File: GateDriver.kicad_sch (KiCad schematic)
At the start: 0 parts

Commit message: add gate driver
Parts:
- added C15: 10nF, symbol Device:C_Small
- added C16, C19: 220nF, symbol Device:C_Small
- added C17: 4.7uF, symbol Device:C_Small
- added C18: 2.2uF, symbol Device:C_Small
- added R28, R31, R32, R34, R35, R36, R37: 1k, symbol Device:R_Small
- added R38, R39: 10k, symbol Device:R_Small
- added U4: 2ED4820EMXUMA2, custom_footprints:2ed4820emxuma2, symbol custom_symbols:2ED4820EMXUMA2
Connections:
- new net: R28.2, U4.1 (SAFESTATEN)
- new net: R36.2, U4.6 (MISO)
- new net: R31.2, U4.2 (INTERRUPT)
- new net: R35.2, U4.5 (MOSI)
- new net: R34.2, R39.1, U4.4 (CSN)
- new net: R32.2, U4.3 (SCLK)
- new net: R37.2, U4.7 (ENABLE)
- new net: C15.1, R38.1
- new net: R38.2, U4.9 (CSO)
- new net +3V3: R39.2, U4.8 (VDD)
- new net BAT+: C16.1, C17.1, C18.2, U4.24 (VBAT)
- new net GATE_A: U4.18 (GA)
- new net GD_EN: R37.1
- new net GD_INT: R31.1
- new net GND: C16.2, C17.2, U4.12 (AGND), U4.13 (GND), U4.19 (CPGND), U4.25 (EPAD)
- new net IS_N: U4.10 (ISN)
- new net IS_P: U4.11 (ISP)
- new net SOURCE_A: U4.17 (SA)
- new net SPI2_MISO: R36.1
- new net SPI2_MOSI: R35.1
- new net SPI2_SCLK: R32.1
- new net cph: C19.2, U4.22 (CPH)
- new net cpl: C19.1, U4.21 (CPL)
- new net vcp: C18.1, U4.23 (VCP)
- new net ~{GD_SAFE}: R28.1
- new net ~{SPI2_CS}: R34.1
- no-connect marks 0 -> 2

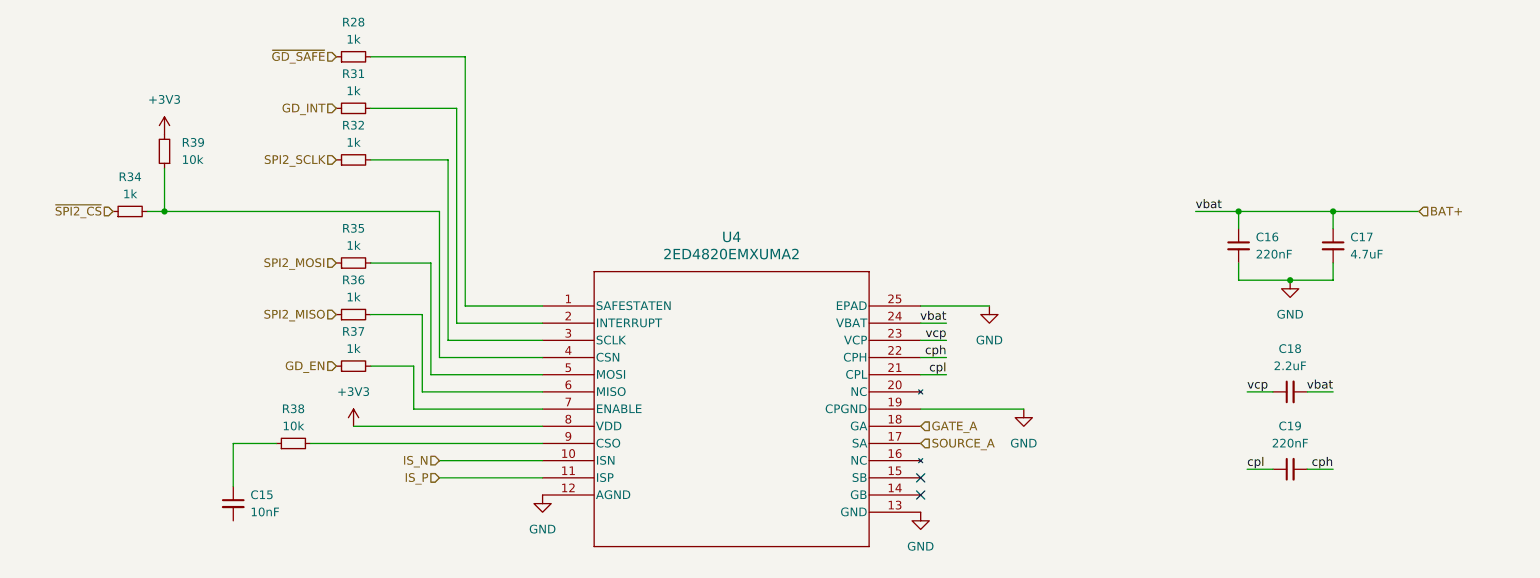
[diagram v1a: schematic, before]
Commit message: finish protection sheet
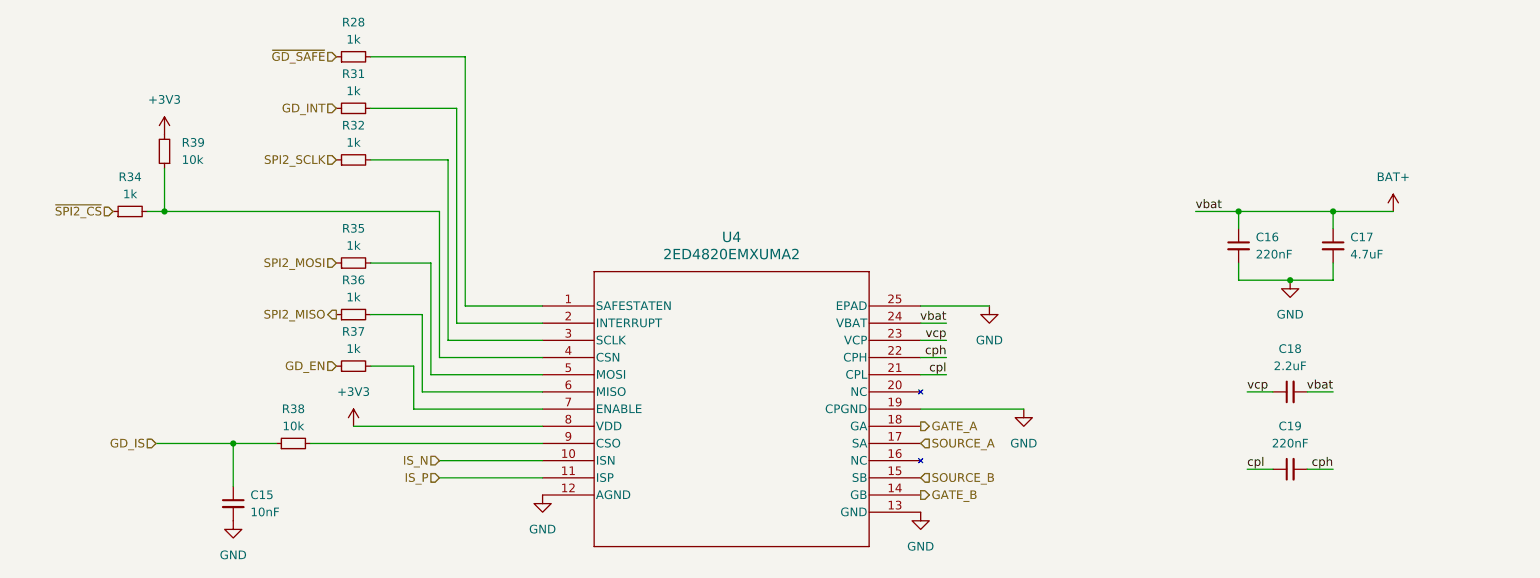
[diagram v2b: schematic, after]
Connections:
- net GND: now also C15.2
- net GD_IS: now reaches C15.1, R38.1
- net GATE_B: now reaches U4.14 (GB)
- net SOURCE_B: now reaches U4.15 (SB)
- no-connect marks 2 -> 0
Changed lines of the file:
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@@
+	)
+	(junction
+		(at 101.6 104.14)
+		(diameter 0)
+		(color 0 0 0 0)
+	)
+	(junction
+		(at 264.16 69.85)
+		(diameter 0)
+		(color 0 0 0 0)
 	)
 	(junction
@@
 	)
 	(junction
-		(at 264.16 69.85)
-		(diameter 0)
-		(color 0 0 0 0)
-	)
-	(junction
 		(at 91.44 69.85)
 		(diameter 0)
@@
 		(color 0 0 0 0)
 	)
-	(no_connect
-		(at 203.2 109.22)
-	)
-	(no_connect
-		(at 203.2 111.76)
-	)
 	(wire
 		(pts
@@
 	(wire
 		(pts
+			(xy 101.6 104.14) (xy 90.17 104.14)
+		)
+		(stroke
+			(width 0)
+			(type default)
+		)
+	)
+	(wire
+		(pts
 			(xy 121.92 46.99) (xy 135.89 46.99)
 		)
@@
 	(wire
 		(pts
+			(xy 121.92 85.09) (xy 129.54 85.09)
+		)
+		(stroke
+			(width 0)
+			(type default)
+		)
+	)
+	(wire
+		(pts
+			(xy 132.08 69.85) (xy 132.08 91.44)
+		)
+		(stroke
+			(width 0)
+			(type default)
+		)
+	)
+	(wire
+		(pts
+			(xy 128.27 92.71) (xy 128.27 99.06)
+		)
+		(stroke
+			(width 0)
+			(type default)
+		)
+	)
+	(wire
+		(pts
+			(xy 250.19 69.85) (xy 250.19 72.39)
+		)
+		(stroke
+			(width 0)
+			(type default)
+		)
+	)
+	(wire
+		(pts
+			(xy 132.08 109.22) (xy 147.32 109.22)
+		)
+		(stroke
+			(width 0)
+			(type default)
+		)
+	)
+	(wire
+		(pts
+			(xy 251.46 96.52) (xy 255.27 96.52)
+		)
+		(stroke
+			(width 0)
+			(type default)
+		)
+	)
+	(wire
+		(pts
+			(xy 134.62 54.61) (xy 134.62 86.36)
+		)
+		(stroke
+			(width 0)
+			(type default)
+		)
+	)
+	(wire
+		(pts
+			(xy 119.38 101.6) (xy 147.32 101.6)
+		)
+		(stroke
+			(width 0)
+			(type default)
+		)
+	)
+	(wire
+		(pts
+			(xy 91.44 63.5) (xy 91.44 69.85)
+		)
+		(stroke
+			(width 0)
+			(type default)
+		)
+	)
+	(wire
+		(pts
+			(xy 129.54 96.52) (xy 147.32 96.52)
+		)
+		(stroke
+			(width 0)
+			(type default)
+		)
+	)
+	(wire
+		(pts
+			(xy 129.54 85.09) (xy 129.54 96.52)
+		)
+		(stroke
+			(width 0)
+			(type default)
+		)
+	)
+	(wire
+		(pts
 			(xy 101.6 104.14) (xy 101.6 110.49)
 		)
@@
 	(wire
 		(pts
-			(xy 121.92 85.09) (xy 129.54 85.09)
-		)
-		(stroke
-			(width 0)
-			(type default)
-		)
-	)
-	(wire
-		(pts
-			(xy 132.08 69.85) (xy 132.08 91.44)
-		)
-		(stroke
-			(width 0)
-			(type default)
-		)
-	)
-	(wire
-		(pts
-			(xy 128.27 92.71) (xy 128.27 99.06)
-		)
-		(stroke
-			(width 0)
-			(type default)
-		)
-	)
-	(wire
-		(pts
-			(xy 250.19 69.85) (xy 250.19 72.39)
-		)
-		(stroke
-			(width 0)
-			(type default)
-		)
-	)
-	(wire
-		(pts
-			(xy 132.08 109.22) (xy 147.32 109.22)
-		)
-		(stroke
-			(width 0)
-			(type default)
-		)
-	)
-	(wire
-		(pts
-			(xy 251.46 96.52) (xy 255.27 96.52)
-		)
-		(stroke
-			(width 0)
-			(type default)
-		)
-	)
-	(wire
-		(pts
-			(xy 134.62 54.61) (xy 134.62 86.36)
-		)
-		(stroke
-			(width 0)
-			(type default)
-		)
-	)
-	(wire
-		(pts
-			(xy 119.38 101.6) (xy 147.32 101.6)
-		)
-		(stroke
-			(width 0)
-			(type default)
-		)
-	)
-	(wire
-		(pts
-			(xy 91.44 63.5) (xy 91.44 69.85)
-		)
-		(stroke
-			(width 0)
-			(type default)
-		)
-	)
-	(wire
-		(pts
-			(xy 129.54 96.52) (xy 147.32 96.52)
-		)
-		(stroke
-			(width 0)
-			(type default)
-		)
-	)
-	(wire
-		(pts
-			(xy 129.54 85.09) (xy 129.54 96.52)
-		)
-		(stroke
-			(width 0)
-			(type default)
-		)
-	)
-	(wire
-		(pts
 			(xy 203.2 99.06) (xy 218.44 99.06)
 		)
@@
 	(wire
 		(pts
+			(xy 273.05 69.85) (xy 264.16 69.85)
+		)
+		(stroke
+			(width 0)
+			(type default)
+		)
+	)
+	(wire
+		(pts
 			(xy 264.16 80.01) (xy 257.81 80.01)
 		)
@@
 		(pts
 			(xy 203.2 93.98) (xy 207.01 93.98)
-		)
-		(stroke
-			(width 0)
-			(type default)
-		)
-	)
-	(wire
-		(pts
-			(xy 264.16 69.85) (xy 276.86 69.85)
 		)
 		(stroke
@@
 	)
 	(hierarchical_label "GATE_A"
-		(shape input)
+		(shape output)
 		(at 203.2 101.6 0)
 		(effects
@@
 		)
 	)
-	(hierarchical_label "BAT+"
+	(hierarchical_label "GD_IS"
 		(shape input)
-		(at 276.86 69.85 0)
+		(at 90.17 104.14 180)
+		(effects
+			(font
+				(size 1.27 1.27)
+			)
+			(justify right)
+		)
+	)
+	(hierarchical_label "GATE_B"
+		(shape output)
+		(at 203.2 111.76 0)
 		(effects
 			(font
@@
 	)
 	(hierarchical_label "SPI2_MISO"
+		(shape output)
+		(at 116.84 85.09 180)
+		(effects
+			(font
+				(size 1.27 1.27)
+			)
+			(justify right)
+		)
+	)
+	(hierarchical_label "SOURCE_B"
 		(shape input)
-		(at 116.84 85.09 180)
-		(effects
-			(font
-				(size 1.27 1.27)
-			)
-			(justify right)
+		(at 203.2 109.22 0)
+		(effects
+			(font
+				(size 1.27 1.27)
+			)
+			(justify left)
 		)
 	)
@@
 	)
 	(symbol
+		(lib_id "power:GND")
+		(at 101.6 115.57 0)
+		(unit 1)
+		(exclude_from_sim no)
+		(in_bom yes)
+		(on_board yes)
+		(dnp no)
+		(fields_autoplaced yes)
+		(property "Reference" "#PWR057"
+			(at 101.6 121.92 0)
+			(effects
+				(font
+					(size 1.27 1.27)
+				)
+				(hide yes)
+			)
+		)
+		(property "Value" "GND"
+			(at 101.6 120.65 0)
+			(effects
+				(font
+					(size 1.27 1.27)
+				)
+			)
+		)
+		(property "Footprint" ""
+			(at 101.6 115.57 0)
+			(effects
+				(font
+					(size 1.27 1.27)
+				)
+				(hide yes)
+			)
+		)
+		(property "Datasheet" ""
+			(at 101.6 115.57 0)
+			(effects
+				(font
+					(size 1.27 1.27)
+				)
+				(hide yes)
+			)
+		)
+		(property "Description" "Power symbol creates a global label with name \"GND\" , ground"
+			(at 101.6 115.57 0)
+			(effects
+				(font
+					(size 1.27 1.27)
+				)
+				(hide yes)
+			)
+		)
+		(pin "1"
+		)
+		(instances
+			(project "battery_protector"
+				(path "/b2975477-3b95-446c-b662-4cca32764c73/b4114c58-5862-440e-b7bf-85e61f2bb435"
+					(reference "#PWR057")
+					(unit 1)
+				)
+			)
+		)
+	)
+	(symbol
 		(lib_id "Device:R_Small")
 		(at 119.38 92.71 90)
@@
 					(unit 1)
 				)
+			)
+		)
+	)
+	(symbol
+		(lib_id "power:+3V3")
+		(at 273.05 69.85 0)
+		(unit 1)
+		(exclude_from_sim no)
+		(in_bom yes)
+		(on_board yes)
+		(dnp no)
+		(fields_autoplaced yes)
+		(property "Reference" "#PWR062"
+			(at 273.05 73.66 0)
+			(effects
+				(font
+					(size 1.27 1.27)
+				)
+				(hide yes)
+			)
+		)
+		(property "Value" "BAT+"
+			(at 273.05 64.77 0)
+			(effects
+				(font
+					(size 1.27 1.27)
+				)
+			)
+		)
+		(property "Footprint" ""
+			(at 273.05 69.85 0)
+			(effects
+				(font
+					(size 1.27 1.27)
+				)
+				(hide yes)
+			)
+		)
+		(property "Datasheet" ""
+			(at 273.05 69.85 0)
+			(effects
+				(font
+					(size 1.27 1.27)
+				)
+				(hide yes)
+			)
+		)
+		(property "Description" "Power symbol creates a global label with name \"+3V3\""
+			(at 273.05 69.85 0)
+			(effects
+				(font
+					(size 1.27 1.27)
+				)
+				(hide yes)
+			)
+		)
+		(pin "1"
+		)
+		(instances
+			(project "battery_protector"
+				(path "/b2975477-3b95-446c-b662-4cca32764c73/b4114c58-5862-440e-b7bf-85e61f2bb435"
+					(reference "#PWR062")
+					(unit 1)
+				)

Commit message: Added footprints to resistors and capacitors, and fixed the mosfets wiring issue (#4)
Jul9th push. Added footprints to resistors and capacitors, and fixed the mosfets wiring issue
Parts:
- C15, C16, C17, C18, C19: footprint (none) -> Capacitor_SMD:C_0603_1608Metric
- R28, R31, R32, R34, R35, R36, R37, R38, R39: footprint (none) -> Resistor_SMD:R_0603_1608Metric
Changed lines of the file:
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@@
 			)
 		)
-		(property "Footprint" ""
+		(property "Footprint" "Capacitor_SMD:C_0603_1608Metric"
 			(at 257.81 107.95 0)
 			(effects
@@
 			)
 		)
-		(property "Footprint" ""
+		(property "Footprint" "Resistor_SMD:R_0603_1608Metric"
 			(at 119.38 46.99 0)
 			(effects
@@
 			)
 		)
-		(property "Footprint" ""
+		(property "Footprint" "Resistor_SMD:R_0603_1608Metric"
 			(at 119.38 85.09 0)
 			(effects
@@
 			)
 		)
-		(property "Footprint" ""
+		(property "Footprint" "Resistor_SMD:R_0603_1608Metric"
 			(at 119.38 54.61 0)
 			(effects
@@
 			)
 		)
-		(property "Footprint" ""
+		(property "Footprint" "Resistor_SMD:R_0603_1608Metric"
 			(at 119.38 77.47 0)
 			(effects
@@
 			)
 		)
-		(property "Footprint" ""
+		(property "Footprint" "Resistor_SMD:R_0603_1608Metric"
 			(at 86.36 69.85 0)
 			(effects
@@
 			)
 		)
-		(property "Footprint" ""
+		(property "Footprint" "Resistor_SMD:R_0603_1608Metric"
 			(at 119.38 62.23 0)
 			(effects
@@
 			)
 		)
-		(property "Footprint" ""
+		(property "Footprint" "Resistor_SMD:R_0603_1608Metric"
 			(at 119.38 92.71 0)
 			(effects
@@
 			)
 		)
-		(property "Footprint" ""
+		(property "Footprint" "Capacitor_SMD:C_0603_1608Metric"
 			(at 101.6 113.03 0)
 			(effects
@@
 			)
 		)
-		(property "Footprint" ""
+		(property "Footprint" "Capacitor_SMD:C_0603_1608Metric"
 			(at 264.16 74.93 0)
 			(effects
@@
 			)
 		)
-		(property "Footprint" ""
+		(property "Footprint" "Resistor_SMD:R_0603_1608Metric"
 			(at 110.49 104.14 0)
 			(effects
@@
 			)
 		)
-		(property "Footprint" ""
+		(property "Footprint" "Resistor_SMD:R_0603_1608Metric"
 			(at 91.44 60.96 0)
 			(effects
@@
 			)
 		)
-		(property "Footprint" ""
+		(property "Footprint" "Capacitor_SMD:C_0603_1608Metric"
 			(at 257.81 96.52 0)
 			(effects
@@
 			)
 		)
-		(property "Footprint" ""
+		(property "Footprint" "Capacitor_SMD:C_0603_1608Metric"
 			(at 250.19 74.93 0)
 			(effects

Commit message: finish schematic
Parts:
- removed R39: 10k, Resistor_SMD:R_0603_1608Metric, symbol Device:R_Small
- renumbered C15 to C17, C16 to C18, C18 to C19, C19 to C20, C17 to C21, R38 to R36, R28 to R37, R31 to R38, R32 to R39, R34 to R40, R35 to R41, R36 to R42, R37 to R43, U4 to U7
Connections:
- net cph renamed CPH
- net cpl renamed CPL
- net vcp renamed VCP
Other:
- moved on the sheet: R37, R38, R39, R40, R41, R42, R43

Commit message: Did some more routing
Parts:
- added C24: 1uF, Capacitor_SMD:C_0603_1608Metric, symbol Device:C_Small
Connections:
- net +3V3: now also C24.1
- net GND: now also C24.2
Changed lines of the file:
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@@
+	(wire
+		(pts
+			(xy 285.75 69.85) (xy 285.75 72.39)
+		)
+		(stroke
+			(width 0)
+			(type default)
+		)
+	)
 	(wire
 		(pts
@@
 		(pts
 			(xy 250.19 77.47) (xy 250.19 80.01)
+		)
+		(stroke
+			(width 0)
+			(type default)
+		)
+	)
+	(wire
+		(pts
+			(xy 285.75 80.01) (xy 285.75 77.47)
 		)
 		(stroke
@@
 	)
 	(symbol
+		(lib_id "power:+3V3")
+		(at 285.75 69.85 0)
+		(unit 1)
+		(exclude_from_sim no)
+		(in_bom yes)
+		(on_board yes)
+		(dnp no)
+		(fields_autoplaced yes)
+		(property "Reference" "#PWR04"
+			(at 285.75 73.66 0)
+			(effects
+				(font
+					(size 1.27 1.27)
+				)
+				(hide yes)
+			)
+		)
+		(property "Value" "+3V3"
+			(at 285.75 64.77 0)
+			(effects
+				(font
+					(size 1.27 1.27)
+				)
+			)
+		)
+		(property "Footprint" ""
+			(at 285.75 69.85 0)
+			(effects
+				(font
+					(size 1.27 1.27)
+				)
+				(hide yes)
+			)
+		)
+		(property "Datasheet" ""
+			(at 285.75 69.85 0)
+			(effects
+				(font
+					(size 1.27 1.27)
+				)
+				(hide yes)
+			)
+		)
+		(property "Description" "Power symbol creates a global label with name \"+3V3\""
+			(at 285.75 69.85 0)
+			(effects
+				(font
+					(size 1.27 1.27)
+				)
+				(hide yes)
+			)
+		)
+		(pin "1"
+		)
+		(instances
+			(project "battery_protector"
+				(path "/b2975477-3b95-446c-b662-4cca32764c73/b4114c58-5862-440e-b7bf-85e61f2bb435"
+					(reference "#PWR04")
+					(unit 1)
+				)
+			)
+		)
+	)
+	(symbol
 		(lib_id "Device:R_Small")
 		(at 124.46 62.23 90)
@@
 	)
 	(symbol
+		(lib_id "power:GND")
+		(at 285.75 80.01 0)
+		(unit 1)
+		(exclude_from_sim no)
+		(in_bom yes)
+		(on_board yes)
+		(dnp no)
+		(fields_autoplaced yes)
+		(property "Reference" "#PWR03"
+			(at 285.75 86.36 0)
+			(effects
+				(font
+					(size 1.27 1.27)
+				)
+				(hide yes)
+			)
+		)
+		(property "Value" "GND"
+			(at 285.75 85.09 0)
+			(effects
+				(font
+					(size 1.27 1.27)
+				)
+			)
+		)
+		(property "Footprint" ""
+			(at 285.75 80.01 0)
+			(effects
+				(font
+					(size 1.27 1.27)
+				)
+				(hide yes)
+			)
+		)
+		(property "Datasheet" ""
+			(at 285.75 80.01 0)
+			(effects
+				(font
+					(size 1.27 1.27)
+				)
+				(hide yes)
+			)
+		)
+		(property "Description" "Power symbol creates a global label with name \"GND\" , ground"
+			(at 285.75 80.01 0)
+			(effects
+				(font
+					(size 1.27 1.27)
+				)
+				(hide yes)
+			)
+		)
+		(pin "1"
+		)
+		(instances
+			(project "battery_protector"
+				(path "/b2975477-3b95-446c-b662-4cca32764c73/b4114c58-5862-440e-b7bf-85e61f2bb435"
+					(reference "#PWR03")
+					(unit 1)
+				)
+			)
+		)
+	)
+	(symbol
 		(lib_id "Device:C_Small")
 		(at 264.16 74.93 0)
@@
 					(unit 1)
 				)
+			)
+		)
+	)
+	(symbol
+		(lib_id "Device:C_Small")
+		(at 285.75 74.93 0)
+		(unit 1)
+		(exclude_from_sim no)
+		(in_bom yes)
+		(on_board yes)
+		(dnp no)
+		(fields_autoplaced yes)
+		(property "Reference" "C24"
+			(at 288.29 73.6662 0)
+			(effects
+				(font
+					(size 1.27 1.27)
+				)
+				(justify left)
+			)
+		)
+		(property "Value" "1uF"
+			(at 288.29 76.2062 0)
+			(effects
+				(font
+					(size 1.27 1.27)
+				)
+				(justify left)
+			)
+		)
+		(property "Footprint" "Capacitor_SMD:C_0603_1608Metric"
+			(at 285.75 74.93 0)
+			(effects
+				(font
+					(size 1.27 1.27)
+				)
+				(hide yes)
+			)
+		)
+		(property "Datasheet" "~"
+			(at 285.75 74.93 0)
+			(effects
+				(font
+					(size 1.27 1.27)
+				)
+				(hide yes)
+			)
+		)
+		(property "Description" "Unpolarized capacitor, small symbol"
+			(at 285.75 74.93 0)
+			(effects
+				(font
+					(size 1.27 1.27)
+				)
+				(hide yes)
+			)
+		)
+		(pin "1"
+		)
+		(pin "2"
+		)
+		(instances
+			(project "battery_protector"
+				(path "/b2975477-3b95-446c-b662-4cca32764c73/b4114c58-5862-440e-b7bf-85e61f2bb435"
+					(reference "C24")
+					(unit 1)
+				)
